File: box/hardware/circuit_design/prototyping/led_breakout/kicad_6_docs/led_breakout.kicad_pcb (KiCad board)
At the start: 2 copper layers, 43.2 x 58.4 mm, 48 parts, among them J1 rpi_port, U1 MAX6969AWG+, U2 MAX6969AWG+

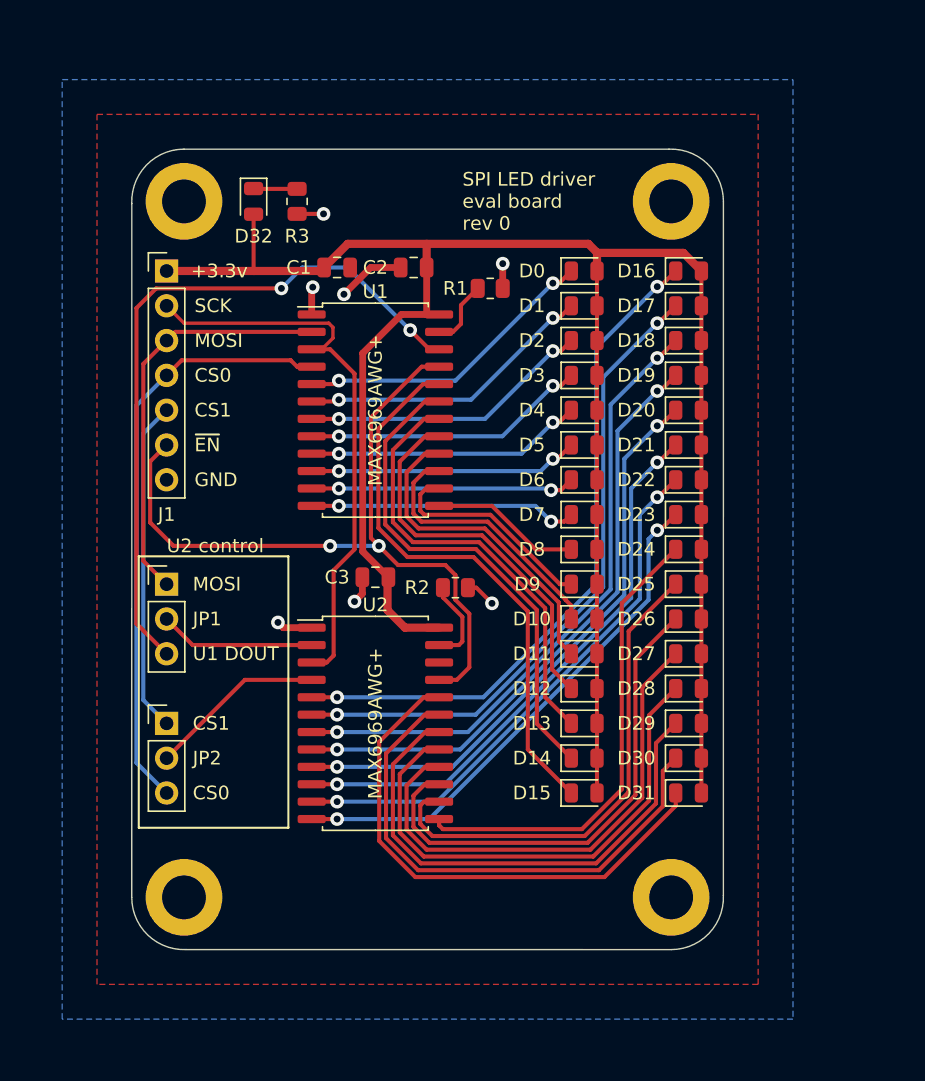
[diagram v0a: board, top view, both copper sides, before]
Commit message: make breakout boards both same size
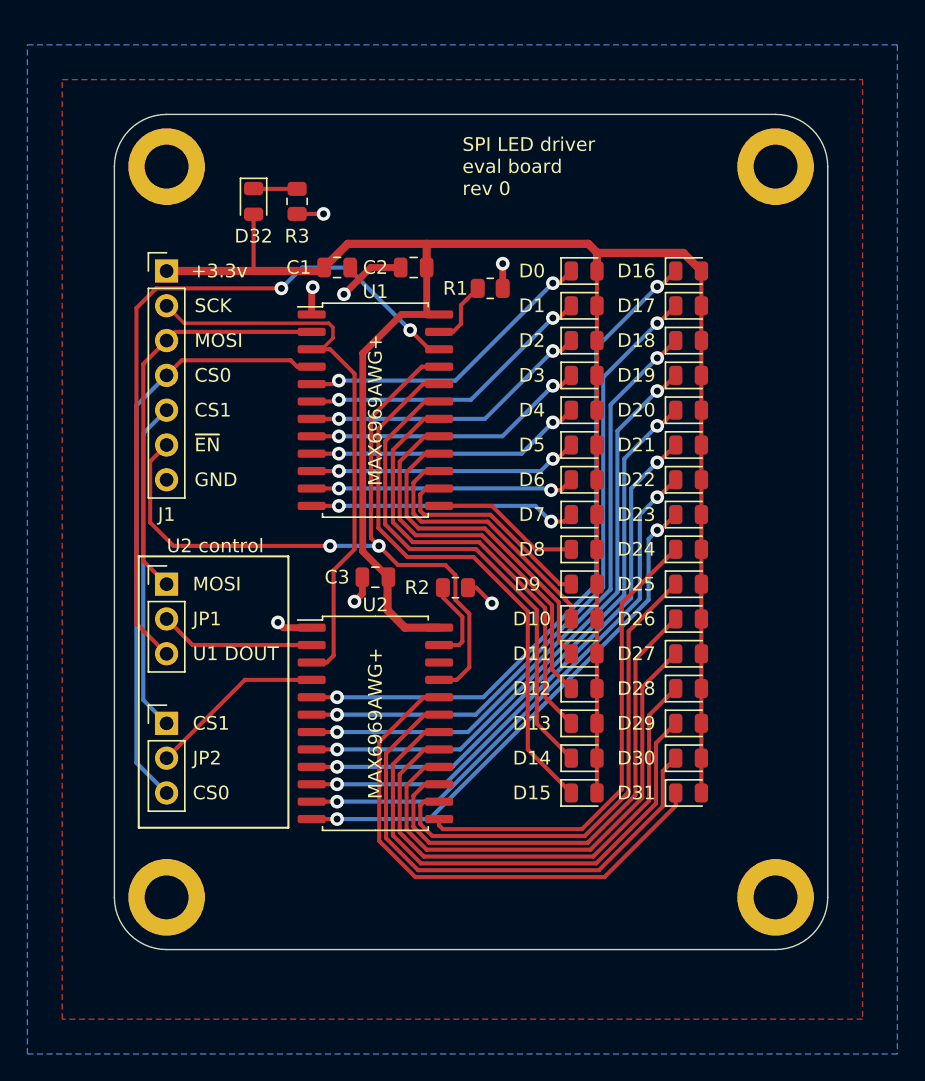
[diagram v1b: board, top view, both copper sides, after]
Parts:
- removed ? (x3): , 
- removed the REF** at (110.5, 35.6)
- added REF**: MountingHole_3.2mm_M3_DIN965_Pad, MountingHole:MountingHole_3.2mm_M3_DIN965_Pad, F.Cu at (109.2, 86.4)
- added REF**: MountingHole_3.2mm_M3_DIN965_Pad, MountingHole:MountingHole_3.2mm_M3_DIN965_Pad, F.Cu at (153.7, 86.4)
- added REF**: MountingHole_3.2mm_M3_DIN965_Pad, MountingHole:MountingHole_3.2mm_M3_DIN965_Pad, F.Cu at (109.2, 33.0)
- added REF**: MountingHole_3.2mm_M3_DIN965_Pad, MountingHole:MountingHole_3.2mm_M3_DIN965_Pad, F.Cu at (153.7, 33.0)
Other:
- board size 43.2 x 58.4 mm -> 52.1 x 61 mm

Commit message: Change LED and switch breakouts, use headers instead of components
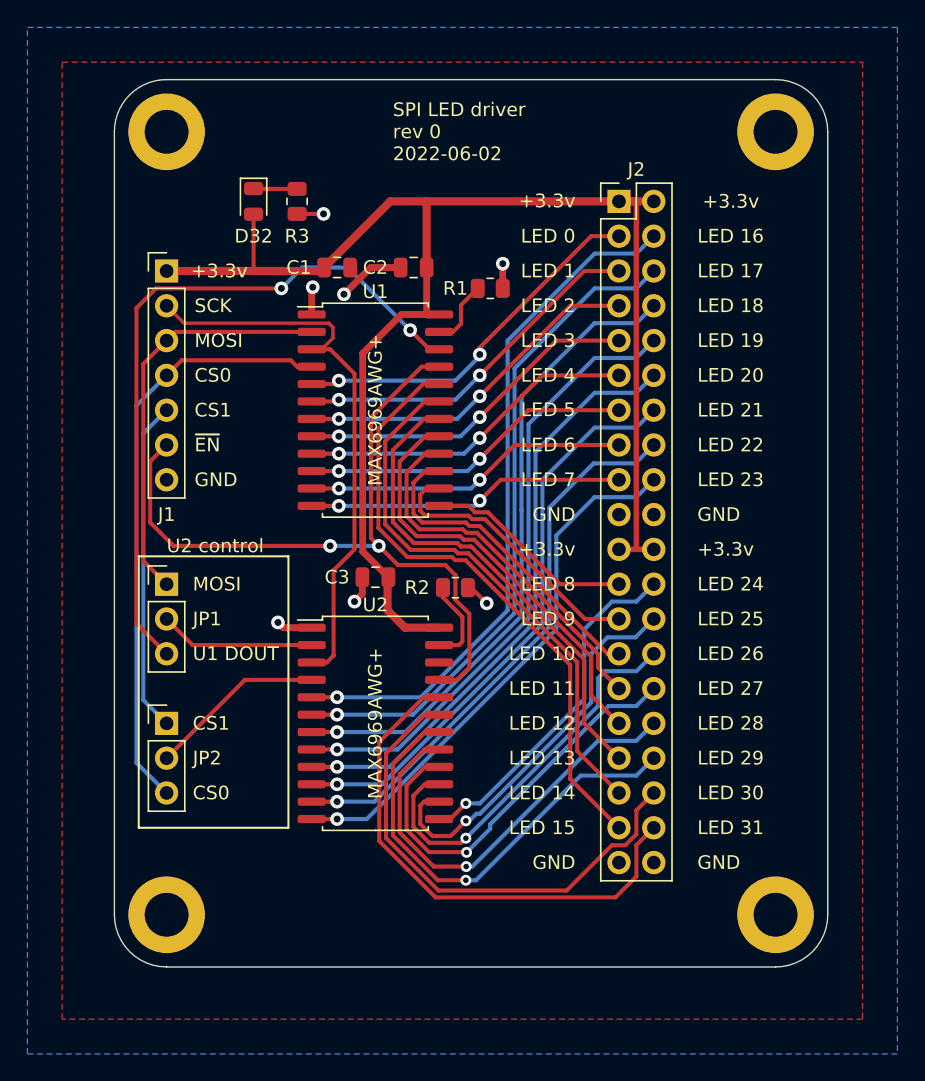
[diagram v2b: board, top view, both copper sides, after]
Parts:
- removed D0, D1, D10, D11, D12, D13, D14, D15, D16, D17, D18, D19, D2, D20, D21, D22, D23, D24, D25, D26, D27, D28, D29, D3, D30, D31, D4, D5, D6, D7, D8, D9: led, LED_SMD:LED_0805_2012Metric
- added J2: LED_header, Connector_PinHeader_2.54mm:PinHeader_2x20_P2.54mm_Vertical, F.Cu at (142.2, 35.6)
- moved REF** 2.54 mm to (153.7, 30.5)
- moved REF** 2.54 mm to (109.2, 30.5)
- moved REF** 1.27 mm to (109.2, 87.6)
- moved REF** 1.27 mm to (153.7, 87.6)
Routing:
- net +3V3: track 158.1 -> 108.7 mm
- net /LED24: track 34.3 -> 25.7 mm, vias 0 -> 1
- net /LED25: track 36.3 -> 28.9 mm, vias 0 -> 1
- net /LED26: track 36.7 -> 29.4 mm, vias 0 -> 1
- net /LED27: track 37.1 -> 30.0 mm, vias 0 -> 1
- net /LED28: track 37.5 -> 31.8 mm, vias 0 -> 1
- net /LED0: track 22.4 -> 27.3 mm
- net /LED8: track 11.0 -> 15.5 mm
- net /LED4: track 20.3 -> 24.8 mm
- net /LED5: track 19.7 -> 24.3 mm
- net /LED2: track 21.3 -> 25.8 mm
- net /LED3: track 20.8 -> 25.3 mm
- net /LED1: track 21.8 -> 26.4 mm
- net /LED9: track 16.0 -> 20.5 mm
- net /LED6: track 19.3 -> 23.7 mm
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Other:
- board size 52.1 x 61 mm -> 52.1 x 64.8 mm
- board text added: "LED 0"
- board text added: "LED 1"
- board text added: "LED 10"
- board text added: "LED 11"
- board text added: "LED 12"
- board text added: "LED 13"
- board text added: "LED 14"
- board text added: "LED 15"
- board text added: "LED 16"
- board text added: "LED 17"
- board text added: "LED 18"
- board text added: "LED 19"
- board text added: "LED 2"
- board text added: "LED 20"
- board text added: "LED 21"
- board text added: "LED 22"
- board text added: "LED 23"
- board text added: "LED 24"
- board text added: "LED 25"
- board text added: "LED 26"
- board text added: "LED 27"
- board text added: "LED 28"
- board text added: "LED 29"
- board text added: "LED 3"
- board text added: "LED 30"
- board text added: "LED 31"
- board text added: "LED 4"
- board text added: "LED 5"
- board text added: "LED 6"
- board text added: "LED 7"
- board text added: "LED 8"
- board text added: "LED 9"
- board text added: "SPI LED driver rev 0 2022-06-02"
- board text removed: "SPI LED driver eval board rev 0"
